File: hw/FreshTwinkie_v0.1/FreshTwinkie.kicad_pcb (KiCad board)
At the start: 2 copper layers, 30.2 x 25 mm, 54 parts, among them J1 USB_C_Receptacle, J2 USB_B_Micro, P1 USB_C_Plug, Q1 BSD840NH6327XTSA1, Q2 BSD840NH6327XTSA1, Q3 BSD840NH6327XTSA1, Q4 BSD840NH6327XTSA1, SW1 SW_Push, U1 AD8606ARMZ-REEL, U2 STM32F072CBUx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

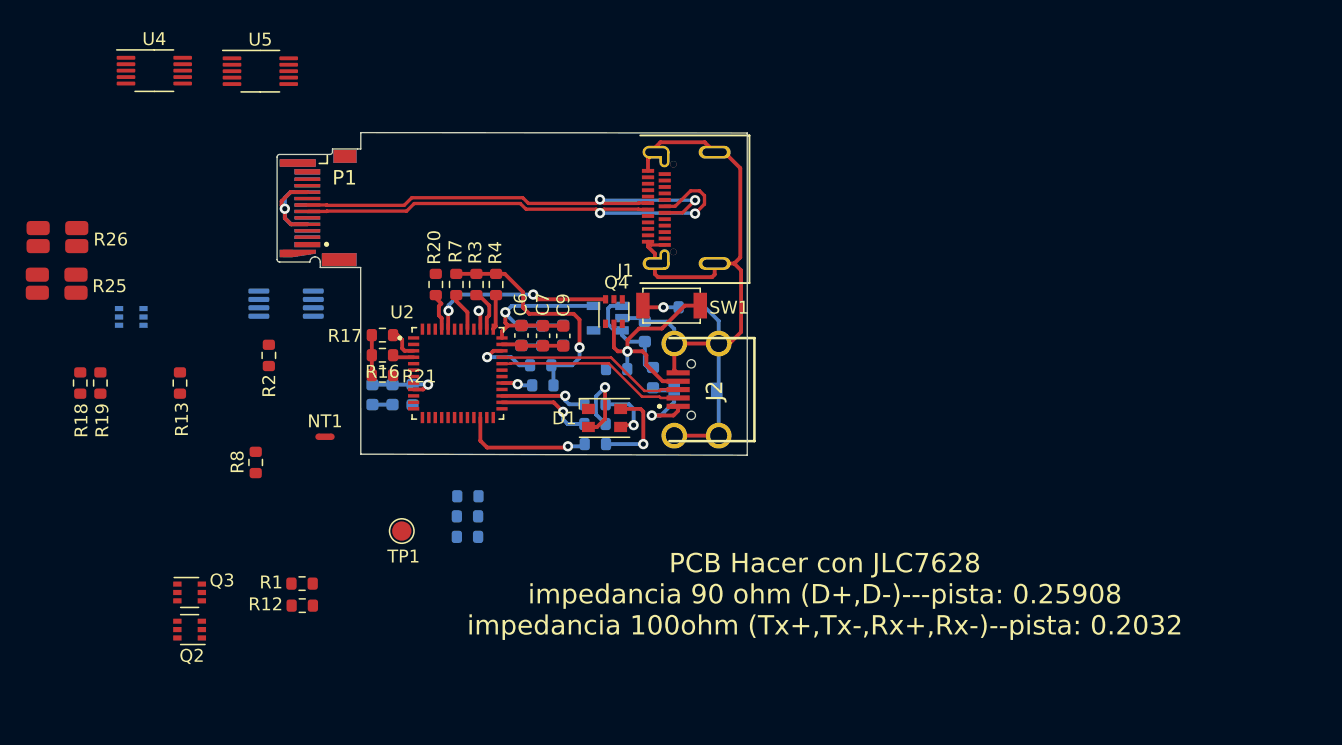
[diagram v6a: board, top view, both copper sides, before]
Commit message: routeU1-5toMc
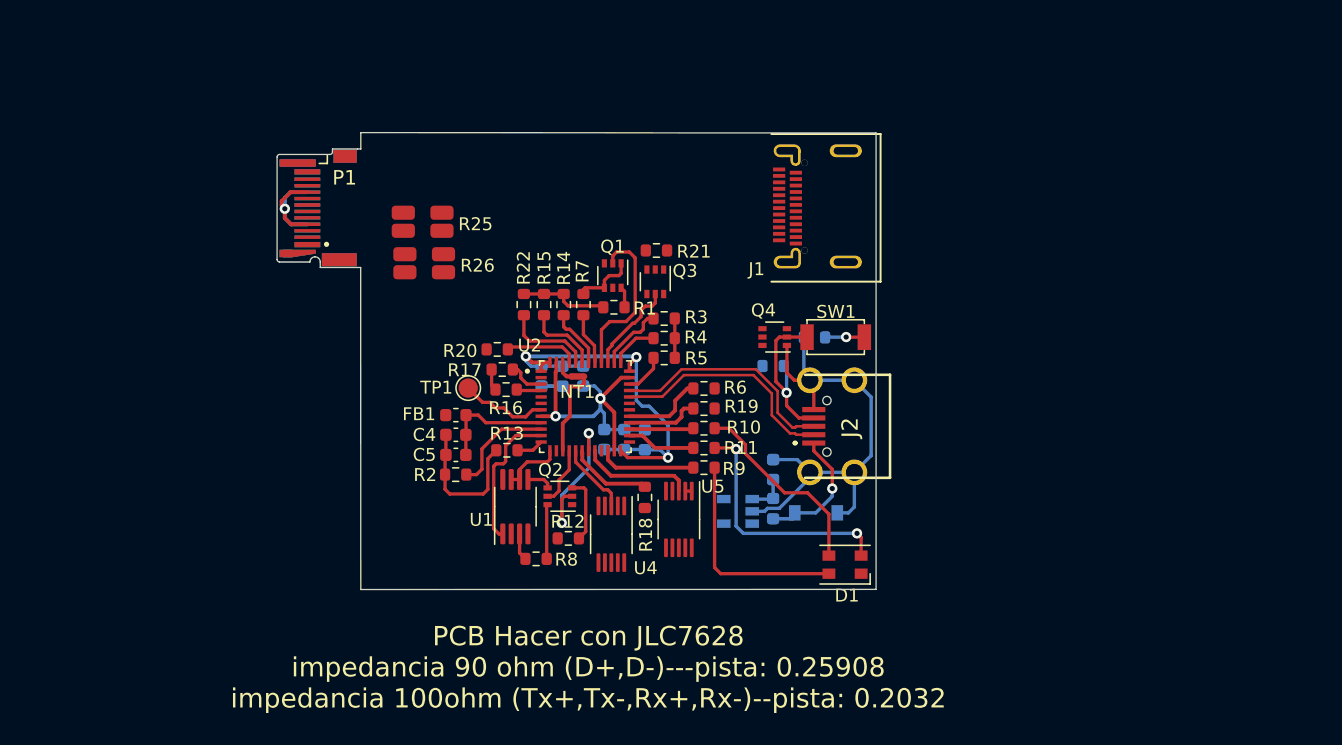
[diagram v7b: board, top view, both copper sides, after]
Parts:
- C4, C5, FB1, R10, R11, R14, R15, R22, R5, R6, R9: moved to F.Cu
- C6, C7, C9: moved to B.Cu
- Q1: value BSD840NH6327XTSA1 -> BSD84; moved to F.Cu
- Q2, Q3, Q4: value BSD840NH6327XTSA1 -> BSD84
- U1: value AD8606ARMZ-REEL -> AD860; moved to F.Cu
- moved U4 50.5 mm to (155.6, 121.2), turned to 270 degrees
- moved U5 47.6 mm to (160.8, 120.1), turned to 270 degrees
- moved R19 46.9 mm to (162.8, 111.5), turned to 0 degrees
- moved R18 44.7 mm to (158.2, 118.4)
- moved Q3 43.5 mm to (159.0, 101.6), turned to 270 degrees
- moved Q1 37.5 mm to (155.7, 101.2), turned to 270 degrees
- moved R1 32.3 mm to (155.8, 103.6), turned to 0 degrees
- moved Q2 30.5 mm to (151.6, 118.3)
- moved R25 28.8 mm to (140.9, 97.0)
- moved R26 28.5 mm to (141.1, 100.2)
- moved R13 25.9 mm to (147.5, 114.7), turned to 180 degrees
- moved U1 23.8 mm to (148.1, 119.1), turned to 90 degrees
- moved R21 23.4 mm to (159.1, 99.2), turned to 180 degrees
- moved R8 23.0 mm to (149.7, 123.2), turned to 0 degrees
- moved D1 21.9 mm to (173.7, 123.6), turned to 180 degrees
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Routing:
- net /USBC_D+: track 40.0 -> 0.00 mm, vias 2 -> 0
- net /USBC_D-: track 37.3 -> 0.00 mm, vias 2 -> 0
- net +3V3: track 18.6 -> 42.9 mm, vias 1 -> 3
- net /CC1_TX_DATA: track 0.00 -> 12.6 mm
- net /CC1_TX_EN: track 0.00 -> 11.9 mm, vias 0 -> 2
- net /CC1_BUF: track 0.00 -> 11.1 mm
- net Net-(D1-Pad2): track 8.10 -> 19.2 mm, vias 1 -> 2
- net Net-(D1-Pad3): track 4.65 -> 15.3 mm, vias 1 -> 0
- net Net-(D1-Pad4): track 7.26 -> 16.8 mm, vias 1 -> 0
- net /VBUS_ALERT_L: track 0.00 -> 8.71 mm
- net /CC1: track 18.8 -> 10.1 mm, vias 1 -> 0
- net /CC1_EN: track 0.00 -> 8.20 mm
- net /BOOT: track 14.6 -> 6.94 mm, vias 2 -> 0
- net /TX_CLKIN: track 0.00 -> 6.96 mm
- net /NRST: track 0.00 -> 6.81 mm
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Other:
- board size 30.2 x 25 mm -> 40.2 x 35.5 mm

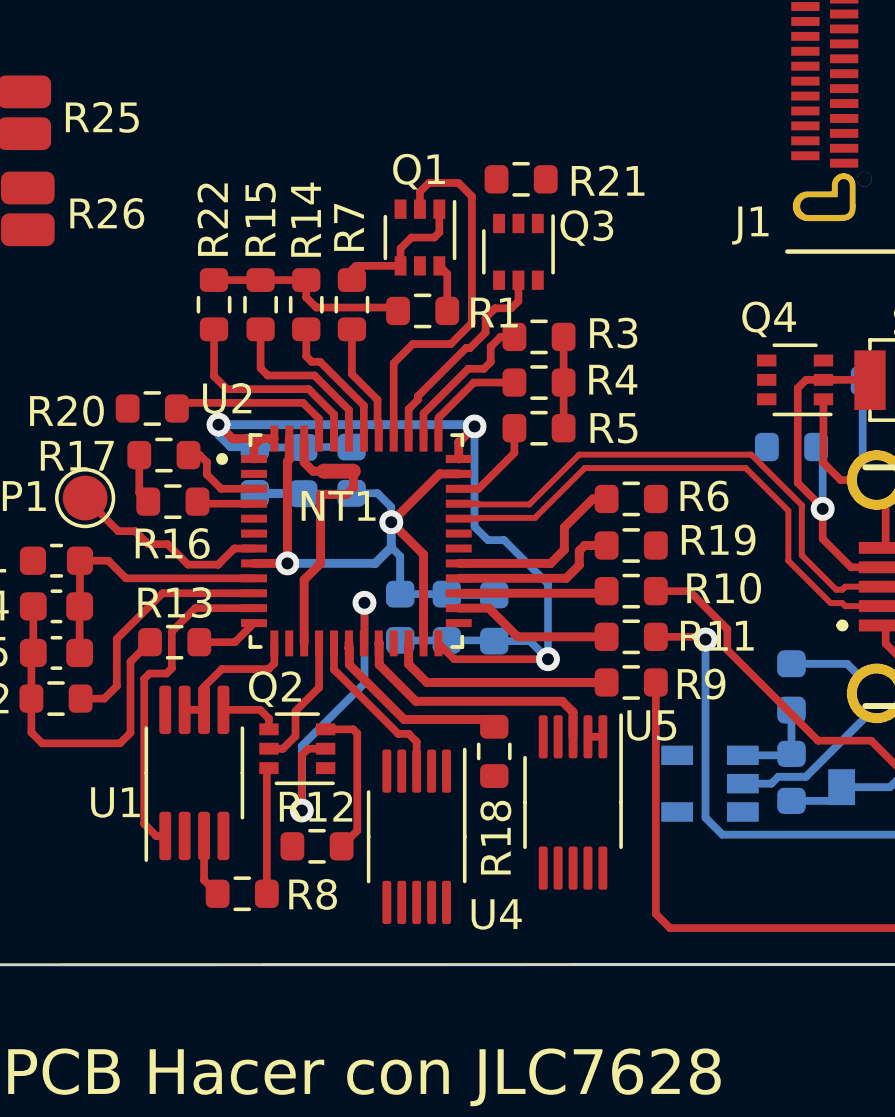
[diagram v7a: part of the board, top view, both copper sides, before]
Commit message: routeR1&R8
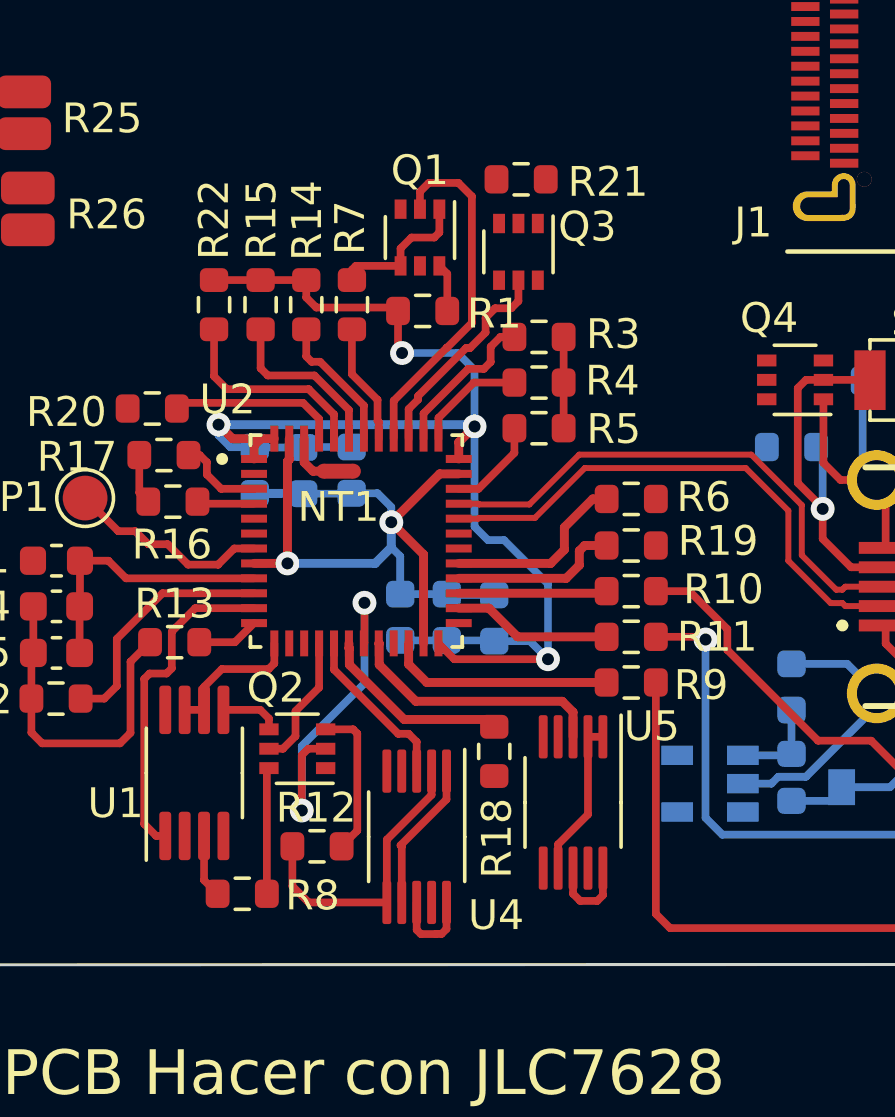
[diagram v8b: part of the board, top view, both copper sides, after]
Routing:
- net +3V3: track 42.9 -> 58.7 mm, vias 3 -> 4
- net GND: track 77.8 -> 87.7 mm
- net /TX_CLKIN: track 6.96 -> 0.00 mm
- net /USBC_VBUS_+: track 0.00 -> 2.95 mm
- net /USBC_CC2_+: track 0.00 -> 2.94 mm
- net /CC1_TX_DATA: track 12.6 -> 11.8 mm
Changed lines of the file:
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@@
     (thickness 0.8)
     (drawings 9)
-    (tracks 366)
+    (tracks 391)
     (zones 0)
     (modules 54)
@@
   (segment (start 146.00091 117.75909) (end 146.00091 115.37409) (width 0.25908) (layer F.Cu) (net 1))
   (segment (start 145.65 118.11) (end 146.00091 117.75909) (width 0.25908) (layer F.Cu) (net 1))
+  (segment (start 161.33 120.492878) (end 161.33 117.89) (width 0.25908) (layer F.Cu) (net 1))
+  (segment (start 160.33 121.492878) (end 161.33 120.492878) (width 0.25908) (layer F.Cu) (net 1))
+  (segment (start 160.33 122.29) (end 160.33 121.492878) (width 0.25908) (layer F.Cu) (net 1))
+  (segment (start 156.59 119.04) (end 156.59 119.986372) (width 0.25908) (layer F.Cu) (net 1))
+  (segment (start 156.59 119.986372) (end 155.04909 121.527282) (width 0.25908) (layer F.Cu) (net 1))
+  (segment (start 155.09 121.568192) (end 155.09 123.44) (width 0.25908) (layer F.Cu) (net 1))
+  (segment (start 155.04909 121.527282) (end 155.09 121.568192) (width 0.25908) (layer F.Cu) (net 1))
   (segment (start 150.14 108.58) (end 150.14 108.13) (width 0.3) (layer F.Cu) (net 2))
   (segment (start 150.37 107.9) (end 150.82 107.9) (width 0.3) (layer F.Cu) (net 2))
@@
   (segment (start 151.89 102.585) (end 150.36 102.585) (width 0.25908) (layer F.Cu) (net 2))
   (segment (start 150.36 102.585) (end 148.8 102.585) (width 0.25908) (layer F.Cu) (net 2))
+  (via (at 155.1 105.03) (size 0.8) (drill 0.4) (layers F.Cu B.Cu) (net 2))
+  (segment (start 154.965 104.895) (end 155.1 105.03) (width 0.25908) (layer F.Cu) (net 2))
+  (segment (start 154.965 103.62) (end 154.965 104.895) (width 0.25908) (layer F.Cu) (net 2))
+  (segment (start 155.1 105.03) (end 156.96 105.03) (width 0.25908) (layer B.Cu) (net 2))
+  (segment (start 157.53 105.6) (end 157.53 107.49) (width 0.25908) (layer B.Cu) (net 2))
+  (segment (start 156.96 105.03) (end 157.53 105.6) (width 0.25908) (layer B.Cu) (net 2))
+  (segment (start 154.59 123.44) (end 151.97 123.44) (width 0.25908) (layer F.Cu) (net 2))
+  (segment (start 151.425 122.895) (end 151.425 121.56) (width 0.25908) (layer F.Cu) (net 2))
+  (segment (start 151.97 123.44) (end 151.425 122.895) (width 0.25908) (layer F.Cu) (net 2))
+  (segment (start 154.59 121.337122) (end 154.59 123.44) (width 0.25908) (layer F.Cu) (net 2))
+  (segment (start 156.09 119.837122) (end 154.59 121.337122) (width 0.25908) (layer F.Cu) (net 2))
+  (segment (start 156.09 119.04) (end 156.09 119.837122) (width 0.25908) (layer F.Cu) (net 2))
   (segment (start 150.14 112.58) (end 145.85 112.58) (width 0.25908) (layer F.Cu) (net 3))
   (segment (start 145.26 111.99) (end 144.3075 111.99) (width 0.25908) (layer F.Cu) (net 3))
@@
   (segment (start 152.116447 108.99) (end 151.82 108.693553) (width 0.3) (layer F.Cu) (net 27))
   (segment (start 152.47 108.99) (end 152.116447 108.99) (width 0.3) (layer F.Cu) (net 27))
-  (segment (start 153.47 108.99) (end 153.47 109.54) (width 0.3) (layer F.Cu) (net 28))
-  (segment (start 153.47 109.54) (end 153.24 109.77) (width 0.3) (layer F.Cu) (net 28))
-  (segment (start 153.24 109.77) (end 152.37 109.77) (width 0.3) (layer F.Cu) (net 28))
-  (segment (start 151.82 112.630002) (end 151.82 114.76) (width 0.3) (layer F.Cu) (net 28))
-  (segment (start 152.37 112.080002) (end 151.82 112.630002) (width 0.3) (layer F.Cu) (net 28))
-  (segment (start 152.37 109.77) (end 152.37 112.080002) (width 0.3) (layer F.Cu) (net 28))
   (segment (start 130.69 94.68) (end 129.99051 95.37949) (width 0.3) (layer F.Cu) (net 29))
   (segment (start 131.99 94.68) (end 130.69 94.68) (width 0.3) (layer F.Cu) (net 29))
@@
   (segment (start 156.35 100.99) (end 156.35 100.21) (width 0.25908) (layer F.Cu) (net 32))
   (segment (start 156.18 101.16) (end 156.35 100.99) (width 0.25908) (layer F.Cu) (net 32))
-  (segment (start 155.7 99.62592) (end 155.99592 99.33) (width 0.25908) (layer F.Cu) (net 33))
-  (segment (start 155.7 100.21) (end 155.7 99.62592) (width 0.25908) (layer F.Cu) (net 33))
-  (segment (start 155.99592 99.33) (end 156.99 99.33) (width 0.25908) (layer F.Cu) (net 33))
-  (segment (start 156.99 99.33) (end 157.44 99.78) (width 0.25908) (layer F.Cu) (net 33))
-  (segment (start 157.44 104.018898) (end 156.728898 104.73) (width 0.25908) (layer F.Cu) (net 33))
-  (segment (start 157.44 99.78) (end 157.44 104.018898) (width 0.25908) (layer F.Cu) (net 33))
-  (segment (start 156.728898 104.73) (end 155.46 104.73) (width 0.25908) (layer F.Cu) (net 33))
-  (segment (start 154.82 105.37) (end 154.82 107.9) (width 0.25908) (layer F.Cu) (net 33))
-  (segment (start 155.46 104.73) (end 154.82 105.37) (width 0.25908) (layer F.Cu) (net 33))
+  (segment (start 155.7 99.62592) (end 155.7 100.21) (width 0.25908) (layer F.Cu) (net 33))
+  (segment (start 156.99 99.33) (end 155.99592 99.33) (width 0.25908) (layer F.Cu) (net 33))
+  (segment (start 157.44 104.018898) (end 157.44 99.78) (width 0.25908) (layer F.Cu) (net 33))
+  (segment (start 156.608898 104.85) (end 157.44 104.018898) (width 0.25908) (layer F.Cu) (net 33))
+  (segment (start 157.44 99.78) (end 156.99 99.33) (width 0.25908) (layer F.Cu) (net 33))
+  (segment (start 156.6 104.85) (end 156.608898 104.85) (width 0.25908) (layer F.Cu) (net 33))
+  (segment (start 155.99592 99.33) (end 155.7 99.62592) (width 0.25908) (layer F.Cu) (net 33))
+  (segment (start 154.82 106.63) (end 156.6 104.85) (width 0.25908) (layer F.Cu) (net 33))
+  (segment (start 154.82 107.9) (end 154.82 106.63) (width 0.25908) (layer F.Cu) (net 33))
   (segment (start 144.33 116.61) (end 145.12182 116.61) (width 0.25908) (layer F.Cu) (net 34))
   (segment (start 145.12182 116.61) (end 145.54182 116.19) (width 0.25908) (layer F.Cu) (net 34))
@@
   (segment (start 172.215 105.93) (end 172.185 105.96) (width 0.25908) (layer B.Cu) (net 59))
   (segment (start 173.82 105.93) (end 172.215 105.93) (width 0.25908) (layer B.Cu) (net 59))
+  (segment (start 161.83 123.2) (end 161.83 122.29) (width 0.25908) (layer F.Cu) (net 61))
+  (segment (start 161.64 123.39) (end 161.83 123.2) (width 0.25908) (layer F.Cu) (net 61))
+  (segment (start 161.07 123.39) (end 161.64 123.39) (width 0.25908) (layer F.Cu) (net 61))
+  (segment (start 160.83 123.15) (end 161.07 123.39) (width 0.25908) (layer F.Cu) (net 61))
+  (segment (start 160.83 122.29) (end 160.83 123.15) (width 0.25908) (layer F.Cu) (net 61))
+  (segment (start 155.59 123.44) (end 155.59 124.36) (width 0.25908) (layer F.Cu) (net 63))
+  (segment (start 155.59 124.36) (end 155.73 124.5) (width 0.25908) (layer F.Cu) (net 63))
+  (segment (start 156.24 124.5) (end 156.24545 124.49455) (width 0.25908) (layer F.Cu) (net 63))
+  (segment (start 155.73 124.5) (end 156.24 124.5) (width 0.25908) (layer F.Cu) (net 63))
+  (segment (start 156.24545 124.49455) (end 156.42545 124.49455) (width 0.25908) (layer F.Cu) (net 63))
+  (segment (start 156.59 124.33) (end 156.59 123.44) (width 0.25908) (layer F.Cu) (net 63))
+  (segment (start 156.42545 124.49455) (end 156.59 124.33) (width 0.25908) (layer F.Cu) (net 63))
   (segment (start 148.93909 112.117736) (end 149.476826 111.58) (width 0.25908) (layer F.Cu) (net 64))
   (segment (start 148.93909 112.12091) (end 148.93909 112.117736) (width 0.25908) (layer F.Cu) (net 64))
